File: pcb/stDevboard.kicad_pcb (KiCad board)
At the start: 4 copper layers, 50 x 100 mm, 151 parts, among them IC1 MPM3610GQV-Z, IC2 IRFR9014PBF, IC3 ICM-45686, IC4 ICM-45686, IC5 MMC5983MA, IC6 AT25SF041B-SSHB-B, J1 battery, J10 73412-0114, J11 USB_C_Receptacle_USB2.0_16P, J12 73412-0114, J13 Conn_01x04, J14 Micro_SD_Card_Det2, J15 Arm, J2 USB_C_Receptacle_USB2.0_16P, J3 Conn_02x03_Top_Bottom, J4 Screw_Terminal_01x12, Q1 DMN3404L, Q2 DMN3404L, Q3 DMN3404L, Q4 DMN3404L, Q5 DMN3404L, Q6 MMBT2222A, Q7 MMBT2222A, Q8 DMN3404L, U1 STM32U073CCUx, U2 STM32U585CIUxQ, U3 BMP581, U4 MAX-M10S, U5 H3LIS331DLTR, Y1 ECS-160-8-36B2-CKM-TR, Y2 CM7V-T1A-32.768KHZ, Y3 ECS-TXO-25CSMV-320-AM-TR, Y4 CM7V-T1A-32.768KHZ

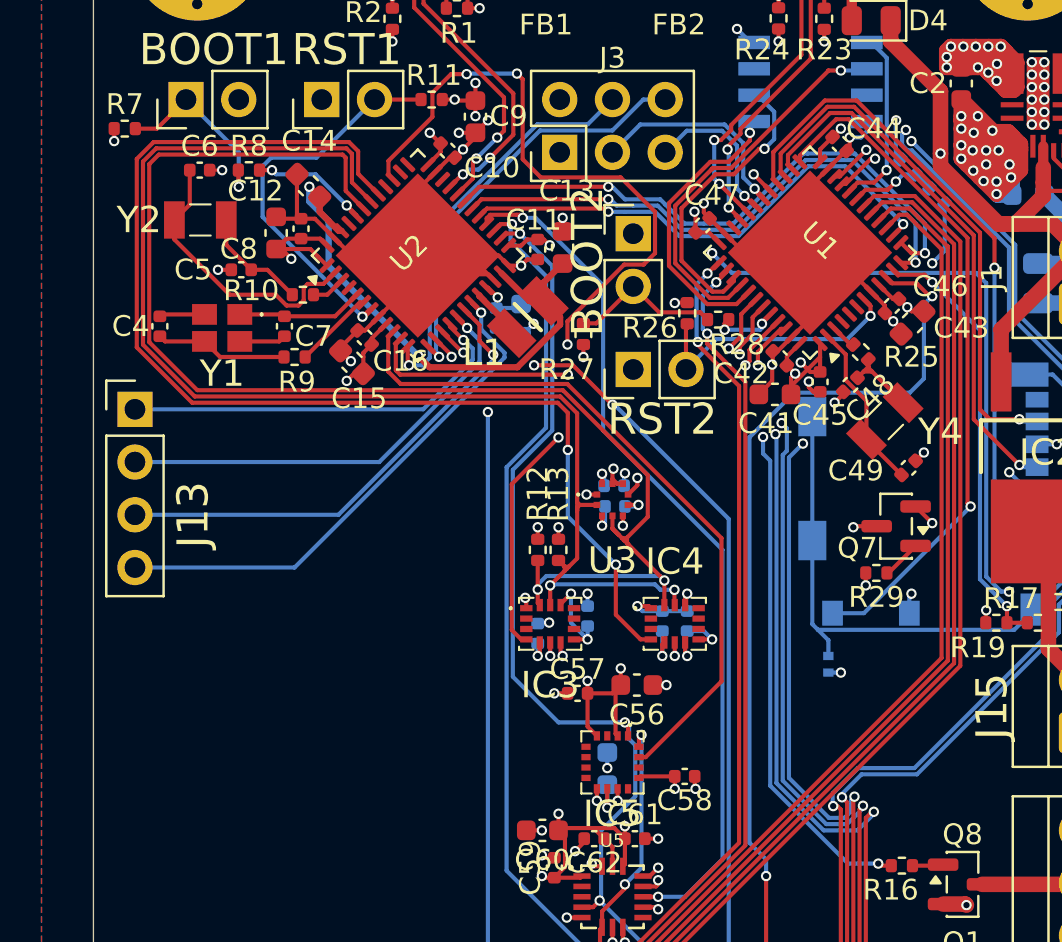
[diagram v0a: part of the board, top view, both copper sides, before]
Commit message: rerouted oscillator stuff - still need to finish i2c routing, also started a platformio board definition
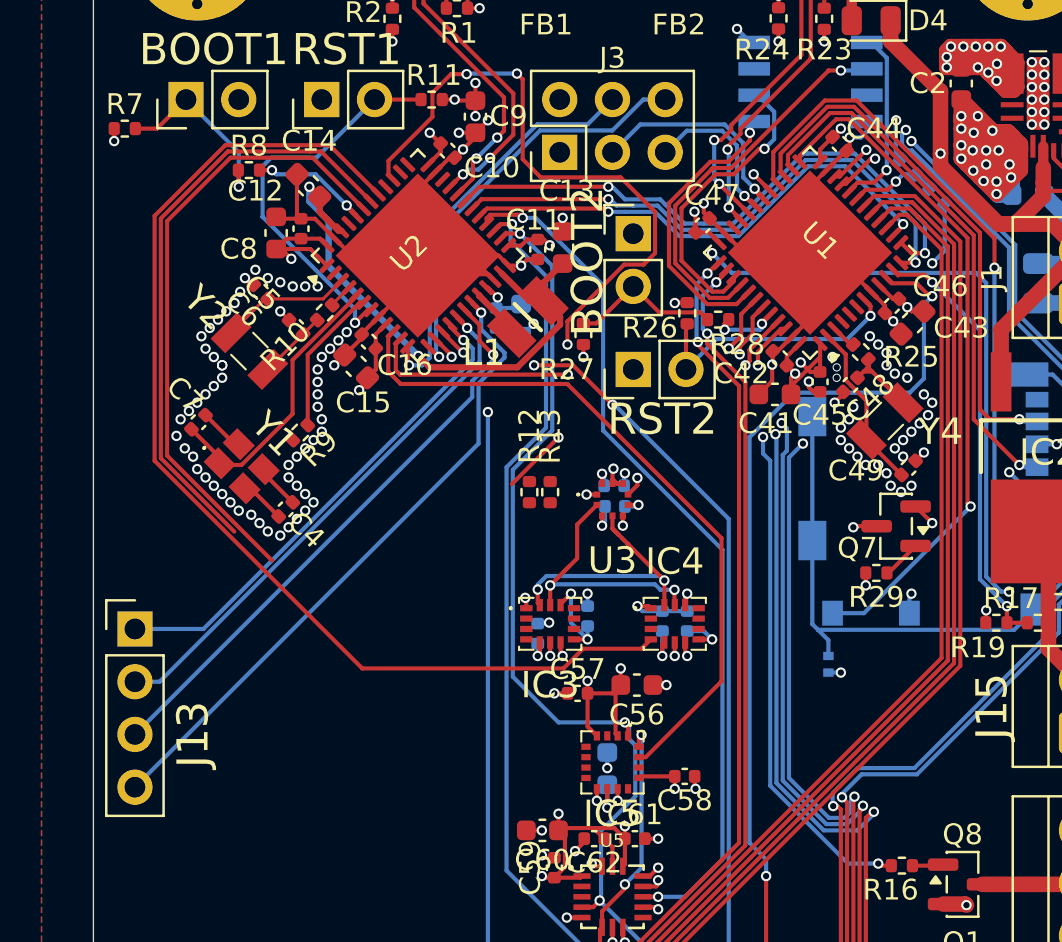
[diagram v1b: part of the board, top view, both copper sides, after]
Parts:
- moved C4 10.7 mm to (109.3, 106.7), turned to -135 degrees
- moved J13 10.6 mm to (102.0, 112.5)
- moved Y2 6.74 mm to (107.5, 99.1), turned to -45 degrees
- moved Y1 6.73 mm to (107.1, 104.7), turned to -45 degrees
- moved C6 6.56 mm to (108.1, 96.3), turned to 135 degrees
- moved C7 6.20 mm to (105.1, 102.5), turned to 45 degrees
- moved C5 3.82 mm to (109.8, 98.0), turned to -45 degrees
- moved R9 3.65 mm to (110.0, 103.0), turned to 45 degrees
- moved R12 2.81 mm to (121.0, 105.9)
- moved R13 2.81 mm to (122.0, 105.9)
- moved R10 1.36 mm to (111.1, 97.3), turned to 45 degrees
- moved C16 0.28 mm to (113.3, 98.7)
- moved C15 0.28 mm to (112.7, 99.9)
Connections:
- C6 pad 1: Net-(U2-PC13) -> Net-(U2-PC14)
- R10 pad 2: Net-(U2-PC14) -> Net-(U2-PC15)
- U2 pad 2: Net-(U2-PC13) -> unconnected-(U2-PC13-Pad2)
- U2 pad 4: unconnected-(U2-PC15-Pad4) -> Net-(U2-PC15)
- U2 pad 40: unconnected-(U2-PB4-Pad40) -> Net-(D1-A)
- Y2 pad 1: Net-(U2-PC13) -> Net-(U2-PC14)
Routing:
- net i2c1_sda: track 66.6 -> 43.5 mm
- net i2c1_sck: track 63.2 -> 41.6 mm
- net Net-(U2-PC13): track 13.7 -> 0.00 mm
- net imu1_int1: track 45.7 -> 37.8 mm
- net Net-(U2-PH0): track 6.08 -> 13.8 mm
- net /main micro/servo4: track 25.3 -> 31.4 mm
- net /main micro/servo3: track 23.3 -> 28.2 mm
- net Net-(U2-PC14): track 1.64 -> 6.37 mm
- net /main micro/servo2: track 21.2 -> 25.6 mm
- net /main micro/servo1: track 19.5 -> 23.9 mm
- net Net-(Y1-OUT/IN): track 6.39 -> 2.18 mm
- net imu2_int1: track 57.7 -> 53.6 mm, vias 2 -> 0
- net Net-(U2-PH1): track 3.91 -> 7.13 mm
- net Net-(C5-Pad2): track 5.37 -> 3.36 mm
- net +3.3V: track 131.7 -> 130.5 mm, vias 64 -> 62
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
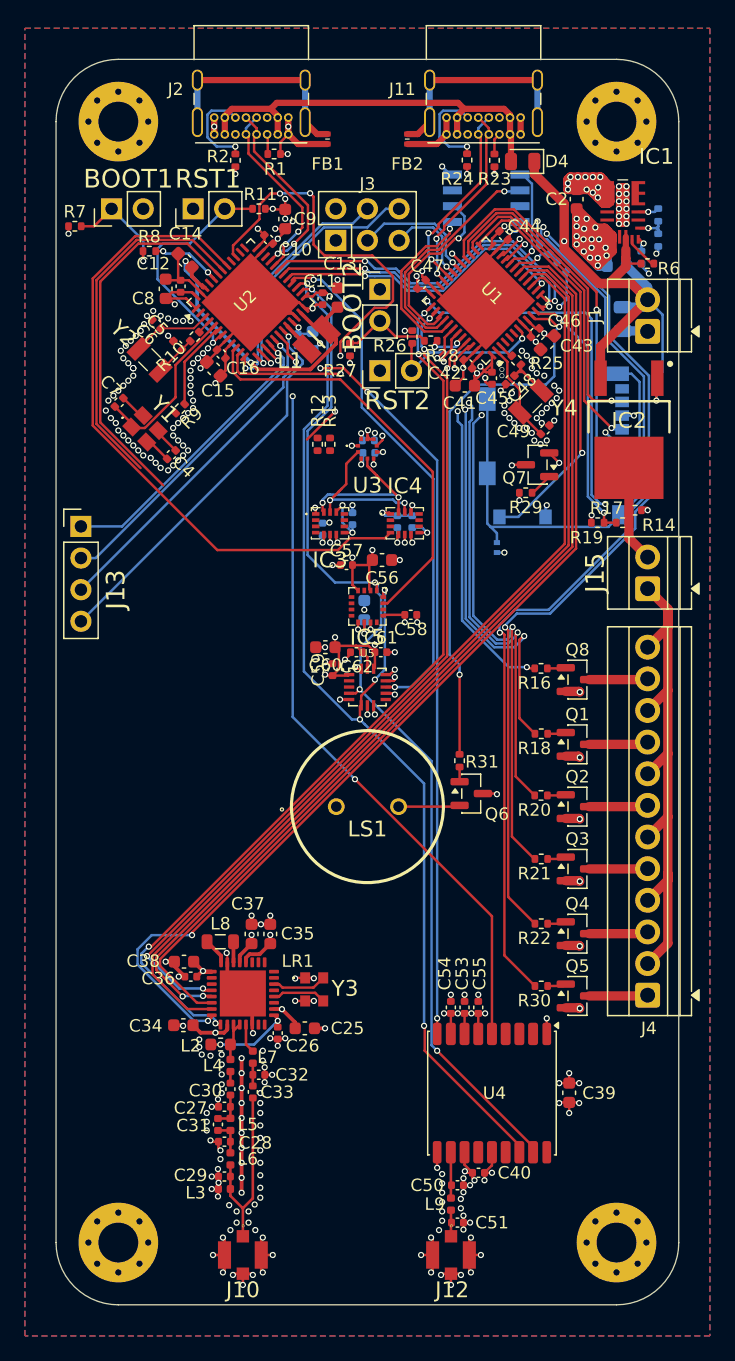
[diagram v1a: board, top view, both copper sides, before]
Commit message: reroute done! except for the gps which I'm currently verifying my implementation on
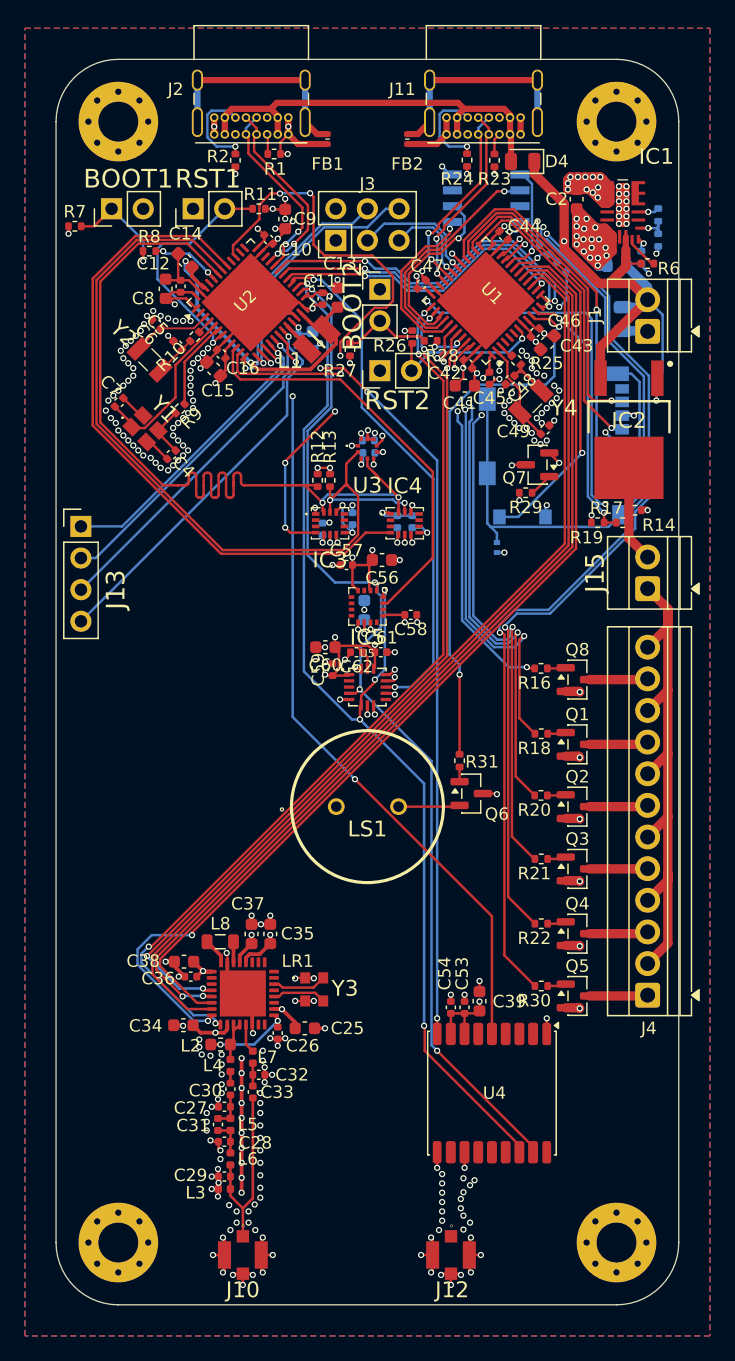
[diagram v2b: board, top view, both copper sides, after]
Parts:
- removed C40, C55: 100nF, Capacitor_SMD:C_0402_1005Metric
- removed C50, C51: C, Capacitor_SMD:C_0402_1005Metric
- removed L9: L, Inductor_SMD:L_0402_1005Metric
- moved C39 10.3 mm to (134.0, 150.6)
- moved R12 2.89 mm to (121.0, 108.8)
- moved R13 2.89 mm to (122.0, 108.8)
- moved C45 0.20 mm to (134.8, 100.6)
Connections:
- U4 pad 11: Net-(U4-RF_IN) -> Net-(J12-SIGNAL)
- U4 pad 14: +3.3V -> unconnected-(U4-VCC_RF-Pad14)
- U4 pad 6: +3.3V -> unconnected-(U4-V_BCKP-Pad6)
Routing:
- net i2c1_sck: track 41.6 -> 68.1 mm
- net i2c1_sda: track 43.5 -> 69.6 mm
- net imu1_int1: track 37.8 -> 48.2 mm, vias 4 -> 6
- net +3.3V: track 130.5 -> 122.3 mm, vias 62 -> 56
- net GND: track 238.8 -> 231.4 mm, vias 292 -> 287
- net Net-(U4-RF_IN): track 3.68 -> 0.00 mm
- net Net-(J12-SIGNAL): track 2.10 -> 0.00 mm
- net Net-(Y1-OUT/IN): track 2.18 -> 4.16 mm

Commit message: board def hopefully done, mpu test firmware written
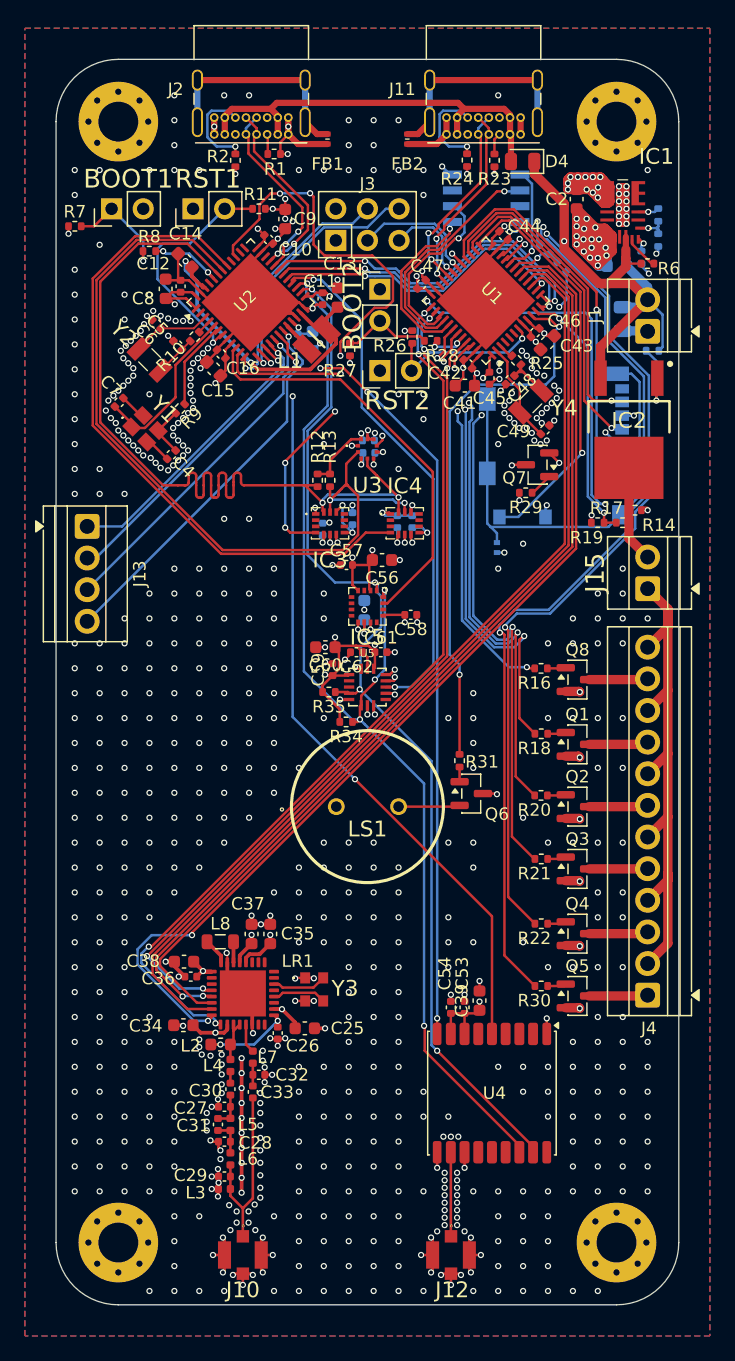
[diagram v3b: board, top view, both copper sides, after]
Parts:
- added R34: 2.7k, Resistor_SMD:R_0402_1005Metric, F.Cu at (123.3, 128.2)
- added R35: 2.7k, Resistor_SMD:R_0402_1005Metric, F.Cu at (121.9, 125.8)
- J13: footprint Connector_PinHeader_2.54mm:PinHeader_1x04_P2.54mm_Vertical -> TerminalBlock:TerminalBlock_Xinya_XY308-2.54-4P_1x04_P2.54mm_Horizontal
- moved R15 2.71 mm to (147.9, 98.4), turned to 0 degrees
- moved J13 0.50 mm to (102.5, 112.5), turned to -90 degrees
- moved C39 0.05 mm to (134.0, 150.6)
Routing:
- net +3.3V: track 122.3 -> 130.3 mm, vias 56 -> 54
- net Net-(J12-SIGNAL): track 0.00 -> 6.75 mm
- net Net-(IC2-G): track 13.9 -> 17.4 mm
- net +BATT: track 51.6 -> 49.4 mm
- net i2c2_sck: track 84.3 -> 85.4 mm
- net i2c2_sda: track 91.7 -> 92.3 mm
- net /main micro/servo1: track 23.8 -> 23.3 mm
- net GND: vias 287 -> 707

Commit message: added models for some things, fixed micro sd impl and a bunch of other stuff - pcb currently probably ready for production
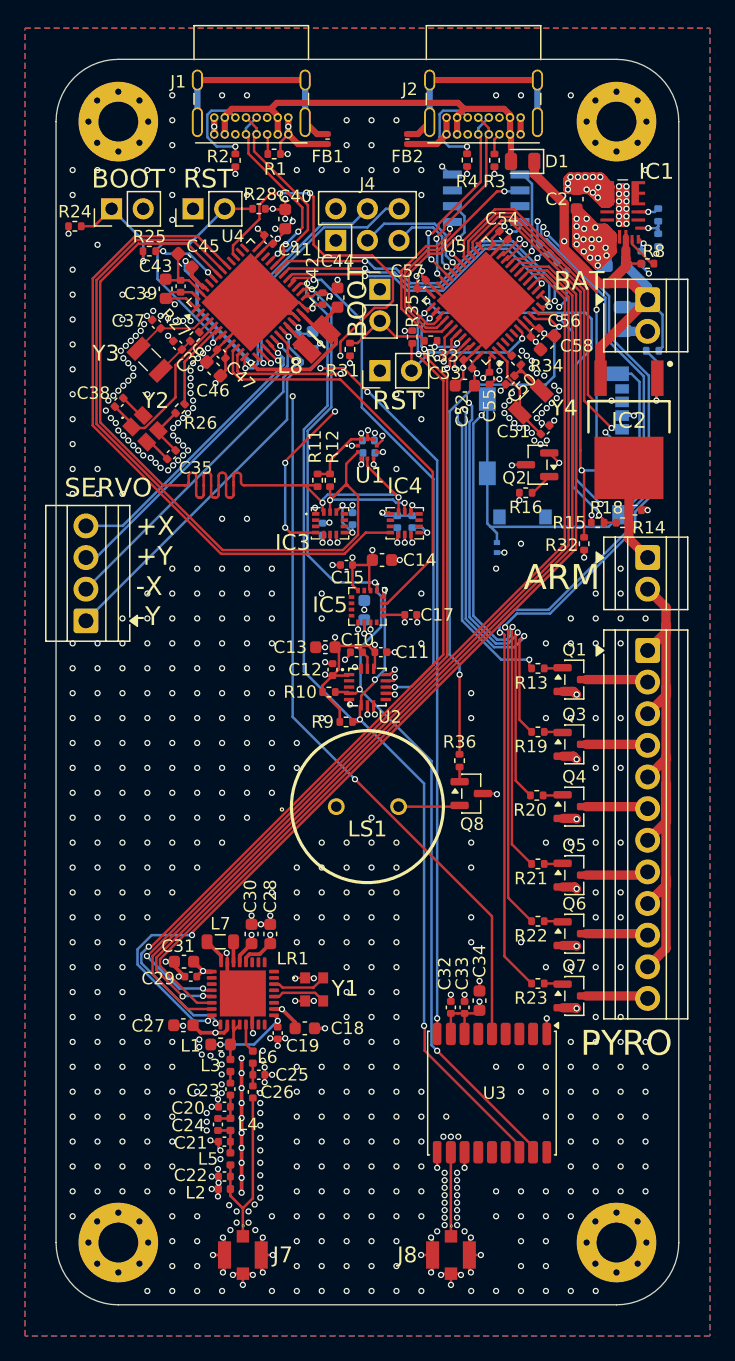
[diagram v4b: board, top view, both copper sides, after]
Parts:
- added R32: 100k, Resistor_SMD:R_0402_1005Metric, F.Cu at (142.4, 113.9)
- C1: value 10uF -> 100uF
- moved PYRO 27.7 mm to (147.5, 122.5), turned to -90 degrees
- moved SERVO 7.58 mm to (102.4, 120.1), turned to 90 degrees
- moved BAT 2.54 mm to (147.5, 94.3), turned to -90 degrees
- moved ARM 2.50 mm to (147.5, 115.0), turned to -90 degrees
- moved Q5 0.56 mm to (141.6, 140.5)
- moved R21 0.48 mm to (138.7, 139.6)
- moved R20 0.34 mm to (138.6, 134.1)
- moved R22 0.34 mm to (138.7, 144.2)
- moved R23 0.34 mm to (138.7, 149.2)
- moved R19 0.31 mm to (138.7, 129.0)
- moved Q1 0.25 mm to (141.6, 124.8)
- moved Q3 0.25 mm to (141.6, 130.0)
- moved Q4 0.25 mm to (141.6, 135.0)
- moved Q6 0.25 mm to (141.6, 145.2)
- moved Q7 0.25 mm to (141.6, 150.2)
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- renumbered J15 to ARM, J1 to BAT, BOOT2 to BOOT, BOOT1 to BOOT, C62 to C10, C61 to C11, C59 to C12, C60 to C13, C56 to C14, C57 to C15, C24 to C16, C58 to C17, C25 to C18, C26 to C19, C27 to C20, C28 to C21, C29 to C22, C30 to C23, C31 to C24, C32 to C25, C33 to C26, C34 to C27, C35 to C28, C36 to C29, C37 to C30, C38 to C31, C54 to C32, C53 to C33, C39 to C34, C4 to C35, C5 to C36, C6 to C37, C7 to C38, C8 to C39, C52 to C4, C9 to C40, C10 to C41, C11 to C42, C12 to C43, C13 to C44, C14 to C45, C15 to C46, C16 to C47, C17 to C48, C18 to C49, C19 to C5, C48 to C50, C49 to C51, C41 to C52, C42 to C53, C44 to C54, C45 to C55, C46 to C56, C47 to C57, C43 to C58, C20 to C6, C21 to C7, C22 to C8, C23 to C9, D4 to D1, J2 to J1, J14 to J10, J11 to J2, J3 to J4, J10 to J7, J12 to J8, L2 to L1, L3 to L2, L4 to L3, L5 to L4, L6 to L5, L7 to L6, L8 to L7, L1 to L8, J4 to PYRO, Q8 to Q1, Q7 to Q2, Q1 to Q3, Q2 to Q4, Q3 to Q5, Q4 to Q6, Q5 to Q7, Q6 to Q8, R35 to R10, R12 to R11, R13 to R12, R16 to R13, R17 to R14, R19 to R15, R29 to R16, R15 to R17, R14 to R18, R18 to R19, R30 to R23, R7 to R24, R8 to R25, R9 to R26, R10 to R27, R11 to R28, R32 to R29, R23 to R3, R33 to R30, R27 to R31, R28 to R33, R25 to R34, R26 to R35, R31 to R36, R24 to R4, R3 to R5, R4 to R6, R5 to R7, R6 to R8, R34 to R9, RST2 to RST, RST1 to RST, J13 to SERVO, U3 to U1, U5 to U2, U4 to U3, U2 to U4, U1 to U5, Y3 to Y1, Y1 to Y2, Y2 to Y3
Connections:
- ARM pad 1: +12C -> Net-(IC2-D)
- ARM pad 2: Net-(IC2-D) -> +12C
- BAT pad 1: GND -> +BATT
- BAT pad 2: +BATT -> GND
- J10 pad 10: /peripheral micro/sd_det -> unconnected-(J10-DET_A-Pad10)
- J10 pad 2: unconnected-(J14-DAT3/CD-Pad2) -> /peripheral micro/sd_cs
- J10 pad 9: +3.3V -> unconnected-(J10-DET_B-Pad9)
- PYRO pad 1: /mosfets/c6_n -> +12C
- PYRO pad 10: +12C -> /mosfets/c5_n
- PYRO pad 11: /mosfets/c1_n -> +12C
- PYRO pad 12: +12C -> /mosfets/c6_n
- PYRO pad 2: +12C -> /mosfets/c1_n
- PYRO pad 3: /mosfets/c5_n -> +12C
- PYRO pad 4: +12C -> /mosfets/c2_n
- PYRO pad 5: /mosfets/c4_n -> +12C
- PYRO pad 6: +12C -> /mosfets/c3_n
- PYRO pad 7: /mosfets/c3_n -> +12C
- PYRO pad 8: +12C -> /mosfets/c4_n
- PYRO pad 9: /mosfets/c2_n -> +12C
- SERVO pad 1: /main micro/servo1 -> /main micro/servo4
- SERVO pad 2: /main micro/servo2 -> /main micro/servo3
- SERVO pad 3: /main micro/servo3 -> /main micro/servo2
- SERVO pad 4: /main micro/servo4 -> /main micro/servo1
- U5 pad 25: /peripheral micro/sd_det -> /peripheral micro/sd_cs
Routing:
- net /peripheral micro/sd_cs: track 0.00 -> 34.6 mm, vias 0 -> 1
- net /peripheral micro/sd_det: track 33.2 -> 0.00 mm, vias 1 -> 0
- net +12C: track 44.9 -> 46.9 mm
- net GND: track 231.4 -> 231.6 mm, vias 707 -> 713
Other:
- board text added: "+1 -1 +2 -2 +3 -3 +4 -4 +5 -5 +6 -6"
- board text added: "+X +Y -X -Y"
